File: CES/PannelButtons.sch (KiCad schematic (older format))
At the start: 12 parts, among them J1501 PannelButtonsConnector, U1501 74HC00, U1502 74HC14

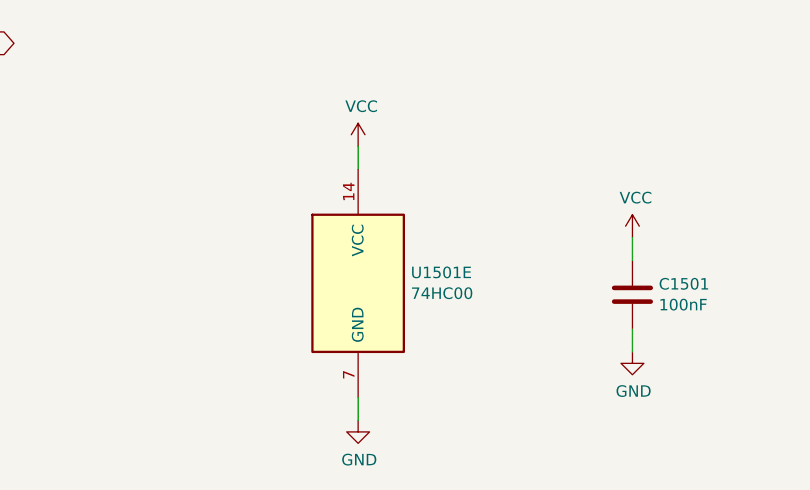
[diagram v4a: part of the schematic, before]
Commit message: Correcting footprints errors
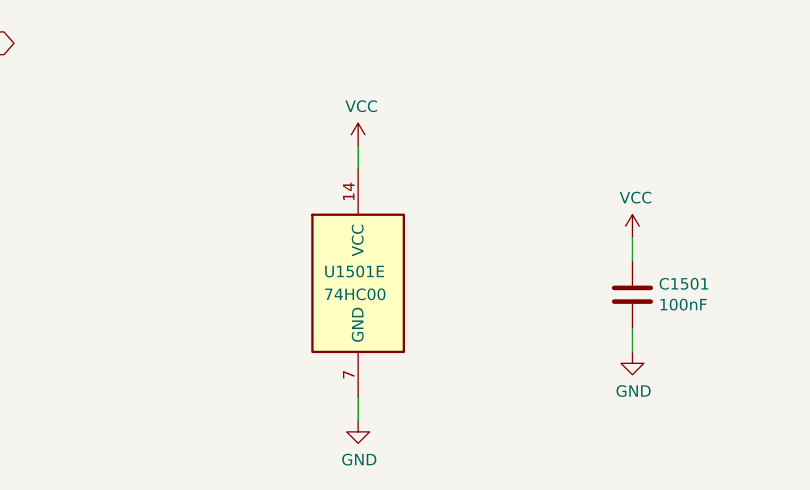
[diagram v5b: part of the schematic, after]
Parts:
- C1501: footprint Capacitor_THT:CP_Radial_D5.0mm_P2.50mm -> Capacitor_THT:C_Disc_D4.3mm_W1.9mm_P5.00mm
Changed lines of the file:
@@
 U 5 1 608648EA
 P 3900 6750
-F 0 "U1501" H 4130 6796 50  0000 L CNN
-F 1 "74HC00" H 4130 6705 50  0000 L CNN
+F 0 "U1501" H 3750 6800 50  0000 L CNN
+F 1 "74HC00" H 3750 6700 50  0000 L CNN
 F 2 "Package_DIP:DIP-14_W7.62mm" H 3900 6750 50  0001 C CNN
 F 3 "http://www.ti.com/lit/gpn/sn74hc00" H 3900 6750 50  0001 C CNN
@@
 $EndComp
 $Comp
-L power:VCC #PWR01511
+L power:VCC #PWR01509
 U 1 1 6086DE5E
 P 4950 2000
-F 0 "#PWR01511" H 4950 1850 50  0001 C CNN
+F 0 "#PWR01509" H 4950 1850 50  0001 C CNN
 F 1 "VCC" H 4965 2173 50  0000 C CNN
 F 2 "" H 4950 2000 50  0001 C CNN
@@
 $EndComp
 $Comp
-L power:VCC #PWR01512
+L power:VCC #PWR01510
 U 1 1 6086E407
 P 4950 2700
-F 0 "#PWR01512" H 4950 2550 50  0001 C CNN
+F 0 "#PWR01510" H 4950 2550 50  0001 C CNN
 F 1 "VCC" H 4965 2873 50  0000 C CNN
 F 2 "" H 4950 2700 50  0001 C CNN
@@
 $EndComp
 $Comp
-L power:VCC #PWR01509
+L power:VCC #PWR01511
 U 1 1 608AAE49
 P 5100 6550
-F 0 "#PWR01509" H 5100 6400 50  0001 C CNN
+F 0 "#PWR01511" H 5100 6400 50  0001 C CNN
 F 1 "VCC" H 5115 6723 50  0000 C CNN
 F 2 "" H 5100 6550 50  0001 C CNN
@@
 $EndComp
 $Comp
-L power:GND #PWR01510
+L power:GND #PWR01512
 U 1 1 608ABC27
 P 5100 7050
-F 0 "#PWR01510" H 5100 6800 50  0001 C CNN
+F 0 "#PWR01512" H 5100 6800 50  0001 C CNN
 F 1 "GND" H 5105 6877 50  0000 C CNN
 F 2 "" H 5100 7050 50  0001 C CNN
@@
 F 0 "C1501" H 5215 6846 50  0000 L CNN
 F 1 "100nF" H 5215 6755 50  0000 L CNN
-F 2 "Capacitor_THT:CP_Radial_D5.0mm_P2.50mm" H 5138 6650 50  0001 C CNN
+F 2 "Capacitor_THT:C_Disc_D4.3mm_W1.9mm_P5.00mm" H 5138 6650 50  0001 C CNN
 F 3 "~" H 5100 6800 50  0001 C CNN
 	1    5100 6800
